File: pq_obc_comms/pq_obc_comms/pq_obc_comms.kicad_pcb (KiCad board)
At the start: 4 copper layers, 40 x 40 mm, 66 parts, among them J1 Conn_01x10, J2 Conn_01x10, J3 Conn_01x10, J4 Conn_01x10, J6 U.FL-R-SMT-1_10_, U1 STM32L476RGTx, U2 SX1262IMLTRT, U3 BD2232G-GTR, U4 BD2232G-GTR, U5 RFswitch, U7 BD2232G-GTR, X1 12MHz, X2 FA-128_32.0000MF20X-K5, X3 32.768KHz

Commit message: obc rework
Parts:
- C1, C10, C11, C12, C2, C4, C5, C6, C7, C8, C9: footprint easyeda:CAPC1005X55N -> Capacitor_SMD:C_0402_1005Metric
- C14, C15, C16, C17, C18: footprint easyeda:CAPC1608X90N -> Capacitor_SMD:C_0603_1608Metric
- C27, C28, C40, C41, C42, C43, C44, C45: footprint easyeda:CAPC1608X90N -> Capacitor_SMD:C_0603_1608Metric; moved to B.Cu
- D1: value VCC -> RBS1LAM40ATR; footprint easyeda:SOD-128_L3.7-W2.5-LS4.7-FD -> Diode_SMD:D_SOD-128; moved to B.Cu
- D2: value VCC_TEST -> RBS1LAM40ATR; footprint easyeda:SOD-128_L3.7-W2.5-LS4.7-FD -> Diode_SMD:D_SOD-128; moved to B.Cu
- J6: value U.FL-R-SMT-1_10_ -> U.FL-R-SMT-1_10; footprint easyeda:U.FL-R-SMT-1(10) -> Connector_Coaxial:U.FL_Hirose_U.FL-R-SMT-1_Vertical
- L1, L3, L4, L5, L6: footprint easyeda:LQW15CNR20J00B -> Inductor_SMD:L_0402_1005Metric
- L2: footprint Resistor_SMD:R_0402_1005Metric -> Inductor_SMD:L_0402_1005Metric
- L7: footprint easyeda:INDC2012X145N -> Inductor_SMD:L_0805_2012Metric
- R3, R4, R6: footprint easyeda:RESC1608X55N -> Resistor_SMD:R_0603_1608Metric
- R7, R8: footprint easyeda:RESC1608X55N -> Resistor_SMD:R_0603_1608Metric; moved to B.Cu
- TP1: renamed from PROBE1; value MS-156C -> CoaxialSwitch_Testpoint; footprint GGS_Connectors:CoaxialSwitch_Hirose_MS-156C3_Horizontal -> Connector_Coaxial:CoaxialSwitch_Hirose_MS-156C3_Horizontal
- U2: footprint easyeda:QFN-24_L4.0-W4.0-P0.50-BL-EP2.6 -> Package_DFN_QFN:QFN-24-1EP_4x4mm_P0.5mm_EP2.6x2.6mm
- U3, U4, U7: footprint easyeda:SSOP-5_L3.0-W1.6-P0.95-LS2.8-TL -> Package_TO_SOT_SMD:SOT-23-5; moved to B.Cu
- U5: value RFswitch -> BGS12PL6E6327XTSA1; footprint easyeda:TSNP-6_L1.1-W0.7-P0.40-BR -> GGS_RF:PG-TSLP-6-4
- X1: value 12MHz -> ECS-120-18-33-JEM-TR3
- X3: value 32.768KHz -> ABS09-32.768KHZ-7-T; footprint easyeda:CRYSTAL-SMD_L4.1-W1.5 -> GGS_Miscellaneous:ABS09; moved to B.Cu
- moved J4 22.9 mm to (110.6, 79.8), turned to -90 degrees
- moved J2 22.9 mm to (82.6, 74.7), turned to 180 degrees
- moved L3 1.03 mm to (108.3, 64.1)
- moved L5 1.03 mm to (104.4, 72.8)
- moved L1 0.99 mm to (108.7, 62.6)
- moved L6 0.95 mm to (106.0, 59.2)
- moved L4 0.94 mm to (108.3, 68.8)
- moved X1 0.16 mm to (85.9, 54.3), turned to -90 degrees
- turned C27 to 0 degrees
- turned C40 to 180 degrees
- turned C41 to 0 degrees
- turned C43 to 0 degrees
- turned C45 to 180 degrees
- turned D1 to 180 degrees
- turned J6 to 180 degrees
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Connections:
- net OSC_OUT renamed /OSC_OUT
- C16 pad 1: VCC_UMBILICAL -> VCC
- C18 pad 1: VCC_UMBILICAL -> VCC
- C31 pad 1: VCC_UMBILICAL -> VCC
- C32 pad 1: VCC_UMBILICAL -> VCC
- C33 pad 1: VCC_UMBILICAL -> VCC
- C34 pad 1: VCC_UMBILICAL -> VCC
- C35 pad 1: VCC_UMBILICAL -> VCC
- C36 pad 1: VCC_UMBILICAL -> VCC
- C37 pad 1: VCC_UMBILICAL -> VCC
- C40 pad 1: unconnected-(C40-Pad1) -> /OSC_IN
- C43 pad 1: VCC_UMBILICAL -> VCC
- C44 pad 1: VCC_UMBILICAL -> VCC
- C45 pad 2: VCC_UMBILICAL -> VCC
- D1 pad 2: VCC_UMBILICAL -> VCC
- D2 pad 1: VCC_TEST2 -> VCC_UMBILICAL
- D2 pad 2: VCC_TEST1 -> VCC
- J1 pad 10: 3V3 -> 3V3_PERM
- J2 pad 1: STM32_PA2 -> SOLAR_X
- J2 pad 10: SOLAR_X -> STM32_PA2
- J2 pad 2: ADC_PL -> unconnected-(J2-Pad2)
- J2 pad 3: DAC_PL -> CLPROG
- J2 pad 4: SWCLK -> CHRGOFF
- J2 pad 5: SWDIO -> NRST
- J2 pad 6: NRST -> SWDIO
- J2 pad 7: CHRGOFF -> SWCLK
- J2 pad 8: CLPROG -> DAC_PL
- J2 pad 9: MPPT_X -> ADC_PL
- J3 pad 10: EPS_RST -> unconnected-(J3-Pad10)
- J3 pad 3: STM32_PD2 -> BATT_NTC
- J4 pad 1: CHRG -> SOLAR_Z
- J4 pad 10: SOLAR_Z -> CHRG
- J4 pad 2: FAULT -> STM32_PD2
- J4 pad 3: VCC_UMBILICAL -> ADCS_POWER
- J4 pad 4: SEL_PH0 -> RST_DRIVERS
- J4 pad 5: P/L_POWER -> ADC_PH
- J4 pad 6: ADC_PH -> P/L_POWER
- J4 pad 7: RST_DRIVERS -> SEL_PH0
- J4 pad 8: MPPT_Y -> VCC_UMBILICAL
- J4 pad 9: MPPT_Z -> FAULT
- J6 pad 1: GND -> Net-(C10-Pad1)
- R4 pad 1: VCC_UMBILICAL -> VCC
- R7 pad 1: VCC_UMBILICAL -> VCC
- R8 pad 1: VCC_UMBILICAL -> VCC
- U1 pad 1: VCC_UMBILICAL -> VCC
- U1 pad 13: VCC_UMBILICAL -> VCC
- U1 pad 19: VCC_UMBILICAL -> VCC
- U1 pad 32: VCC_UMBILICAL -> VCC
- U1 pad 48: VCC_UMBILICAL -> VCC
- U1 pad 5: OSC_IN -> /OSC_IN
- U1 pad 64: VCC_UMBILICAL -> VCC
- U2 pad 1: VCC_UMBILICAL -> VCC
- U2 pad 10: VCC_UMBILICAL -> VCC
- U2 pad 11: VCC_UMBILICAL -> VCC
- U3 pad 1: VCC_UMBILICAL -> VCC
- U4 pad 1: VCC_UMBILICAL -> VCC
- U4 pad 5: P/L2BURN -> ADCS_POWER
- U7 pad 1: VCC_UMBILICAL -> VCC
- X1 pad 1: OSC_IN -> /OSC_IN
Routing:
- net VCC_UMBILICAL: track 149.6 -> 2.70 mm, vias 5 -> 0
- net VCC: track 0.00 -> 138.6 mm, vias 0 -> 5
- net SOLAR_Z: track 0.00 -> 37.1 mm
- net EPS_RST: track 37.1 -> 0.00 mm
- net ADCS_POWER: track 0.00 -> 25.3 mm
- net STM32_PD2: track 25.3 -> 49.0 mm
- net MPPT_Z: track 23.8 -> 0.00 mm
- net MPPT_Y: track 21.8 -> 0.00 mm
- net CHRGOFF: track 14.6 -> 0.00 mm, vias 1 -> 0
- net CHGOFF: track 0.00 -> 14.6 mm, vias 0 -> 1
- net 3V3: track 0.00 -> 8.38 mm
- net OSC32_IN: track 15.0 -> 7.01 mm, vias 2 -> 1
- net /OSC_IN: track 0.00 -> 7.98 mm, vias 0 -> 1
- net STM32_PA15: track 3.45 -> 0.00 mm
- net GND: track 7.92 -> 6.07 mm, vias 59 -> 58
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
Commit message: OBC board revision 3 finished
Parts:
- added C3: 100nF, Capacitor_SMD:C_0603_1608Metric, F.Cu at (104.1, 48.5)
- C27, C28, C31, C32, C33, C34, C35, C36, C37, R7, R8: moved to F.Cu
- X2: footprint easyeda:FA128320000MF20XK5 -> GGS_Miscellaneous:EPSON_FA128
- moved C27 26.5 mm to (112.4, 47.4)
- moved X2 26.3 mm to (112.4, 49.7), turned to -90 degrees
- moved C35 25.6 mm to (100.1, 51.3), turned to 0 degrees
- moved C36 24.0 mm to (87.4, 51.3)
- moved C28 23.5 mm to (112.4, 52.0), turned to 180 degrees
- moved C34 22.9 mm to (87.4, 49.8)
- moved U4 22.2 mm to (104.4, 72.1), turned to -90 degrees
- moved C44 18.5 mm to (104.2, 69.3), turned to 0 degrees
- moved C37 17.7 mm to (100.0, 63.5), turned to 0 degrees
- moved C38 10.8 mm to (86.4, 48.9), turned to 90 degrees
- moved C39 9.50 mm to (92.7, 48.9)
- moved C41 8.53 mm to (94.3, 55.9), turned to 90 degrees
- moved X3 8.06 mm to (89.5, 49.7), turned to 0 degrees
- moved C43 7.71 mm to (108.7, 69.3)
- moved D1 5.96 mm to (109.2, 46.8)
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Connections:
- net Net-(R3-Pad1) renamed /DIO2
- net Net-(U5-Pad4) renamed /RFswitch_Vcc
- D1 pad 1: 3V3 -> 3V3_PERM
- J3 pad 10: unconnected-(J3-Pad10) -> GND
- J4 pad 2: STM32_PD2 -> STM32_PB0
- U1 pad 10: SEL_PH3 -> SEL_PH0
- U1 pad 11: /PoL_P/L_EN -> unconnected-(U1-Pad11)
- U1 pad 22: MPPT_X -> unconnected-(U1-Pad22)
- U1 pad 23: MPPT_Z -> /PoL_ADCS_POWER_EN
- U1 pad 26: EPS_RST -> STM32_PB0
- U1 pad 27: MPPT_Y -> unconnected-(U1-Pad27)
- U1 pad 37: unconnected-(U1-Pad37) -> /PoL_P/L_EN
- U1 pad 41: /BUSY -> /SX1262_BUSY
- U1 pad 54: STM32_PD2 -> unconnected-(U1-Pad54)
- U1 pad 8: CHGOFF -> CHRGOFF
- U4 pad 3: P/L2BURN_OBC -> /PoL_ADCS_POWER_EN
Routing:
- net VCC: track 138.6 -> 63.3 mm, vias 5 -> 18
- net STM32_PD2: track 49.0 -> 0.00 mm, vias 1 -> 0
- net /XTB: track 48.8 -> 9.60 mm, vias 2 -> 0
- net SOLAR_Z: track 37.1 -> 0.00 mm
- net unconnected-(U1-Pad17): track 33.5 -> 0.00 mm, vias 2 -> 0
- net STM32_PB0: track 0.00 -> 32.9 mm, vias 0 -> 2
- net STM32_PA15: track 0.00 -> 25.9 mm, vias 0 -> 2
- net /PoL_ADCS_POWER_EN: track 0.00 -> 25.9 mm, vias 0 -> 1
- net ADCS_POWER: track 25.3 -> 4.79 mm
- net /PoL_P/L_EN: track 34.2 -> 17.0 mm, vias 2 -> 3
- net /XTA: track 23.5 -> 6.70 mm, vias 2 -> 0
- net P/L2BURN_OBC: track 16.5 -> 0.00 mm, vias 1 -> 0
- net CHGOFF: track 14.6 -> 0.00 mm, vias 1 -> 0
- net /DIO2: track 19.4 -> 33.4 mm, vias 2 -> 3
- net MPPT_X: track 14.0 -> 0.00 mm
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- added copper zone on B.Cu, net VCC
- added copper zone on In2.Cu, net VCC
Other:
- board text removed: "12MHz"
- board text removed: "32.7KHz"
- board text removed: "32MHz"
- board text removed: "BD2232G"
- board text removed: "BurnCOMMS"
- board text removed: "D-VCC"
- board text removed: "D-VCCTest"
- board text removed: "OBC-COMMS"
- board text removed: "PL2BURN"
- board text removed: "PL2VCC"
- board text removed: "STM32L162RE"
- board text removed: "SX1262"

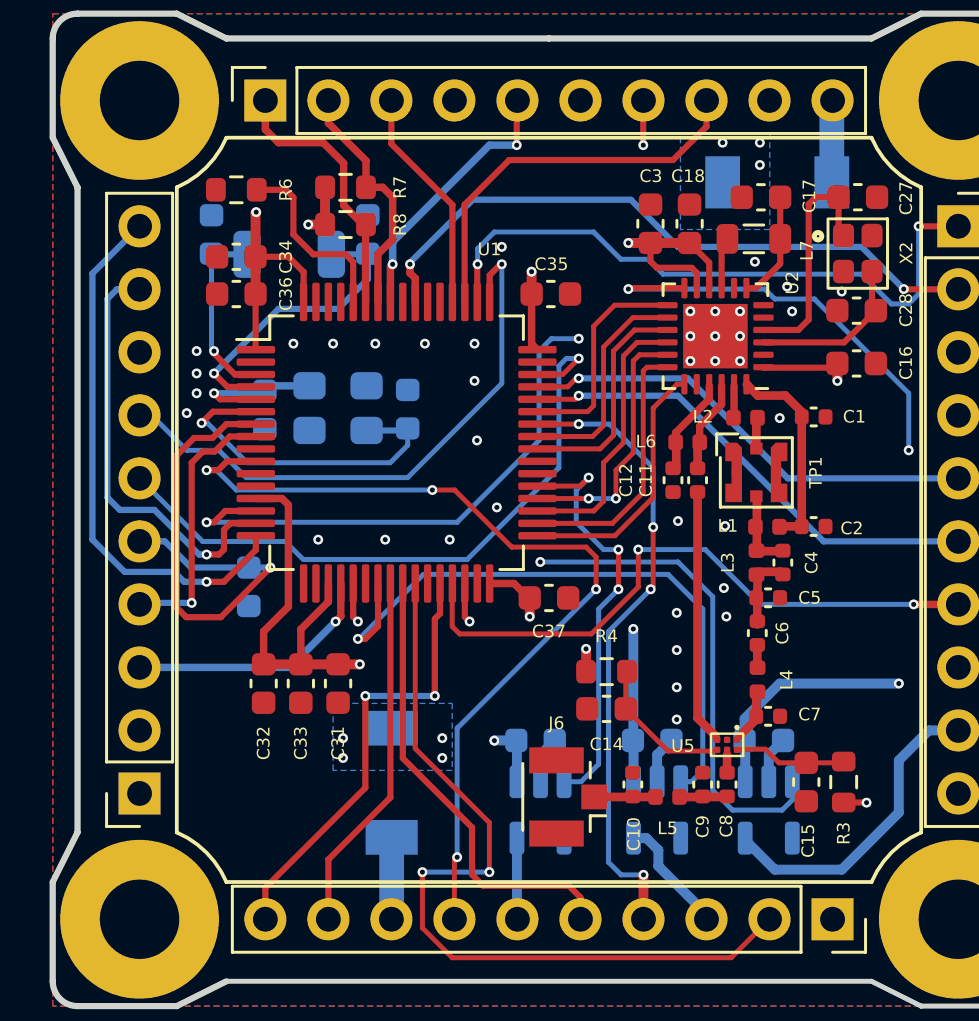
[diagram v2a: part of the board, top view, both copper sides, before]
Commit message: added PA3 pin to pinout
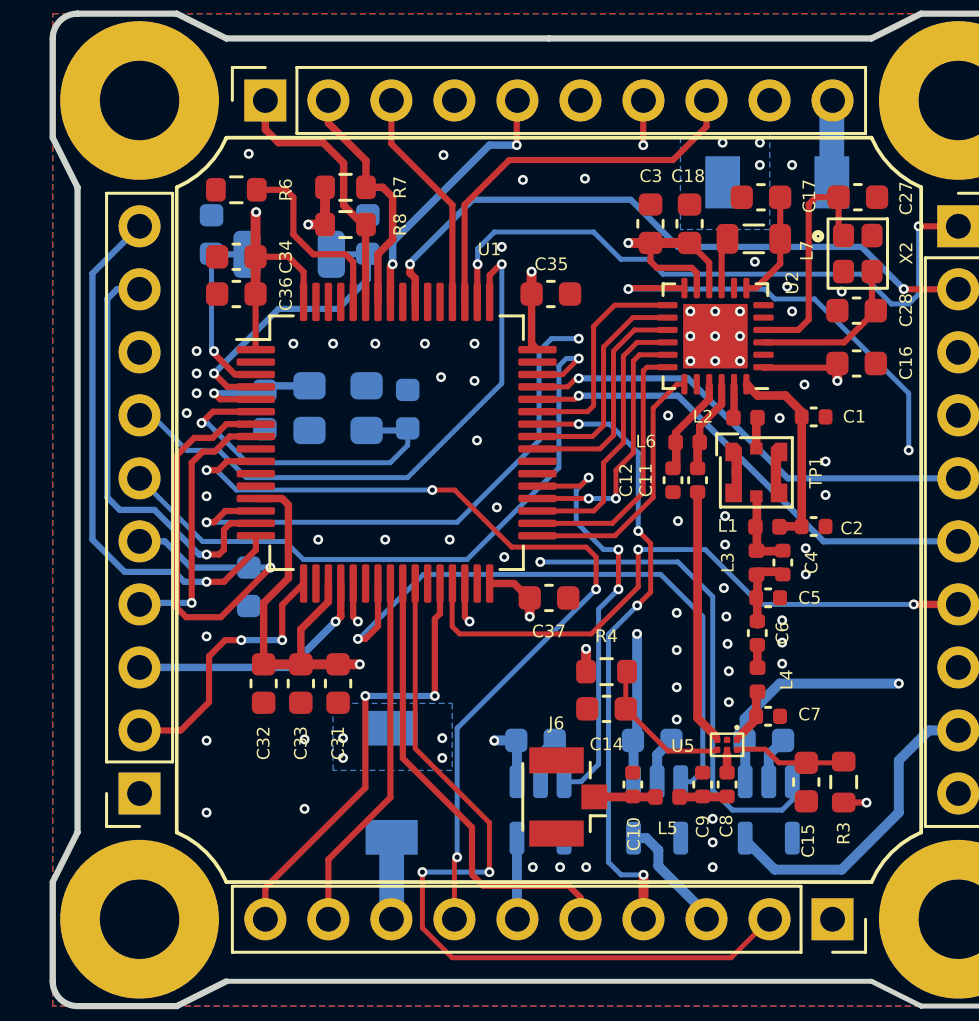
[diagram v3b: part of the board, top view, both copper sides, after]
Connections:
- J2 pad 2: unconnected-(J2-Pad2) -> STM32_PA3
- U1 pad 17: unconnected-(U1-Pad17) -> STM32_PA3
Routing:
- net STM32_PA3: track 0.00 -> 11.0 mm, vias 0 -> 2
- net GND: vias 38 -> 70

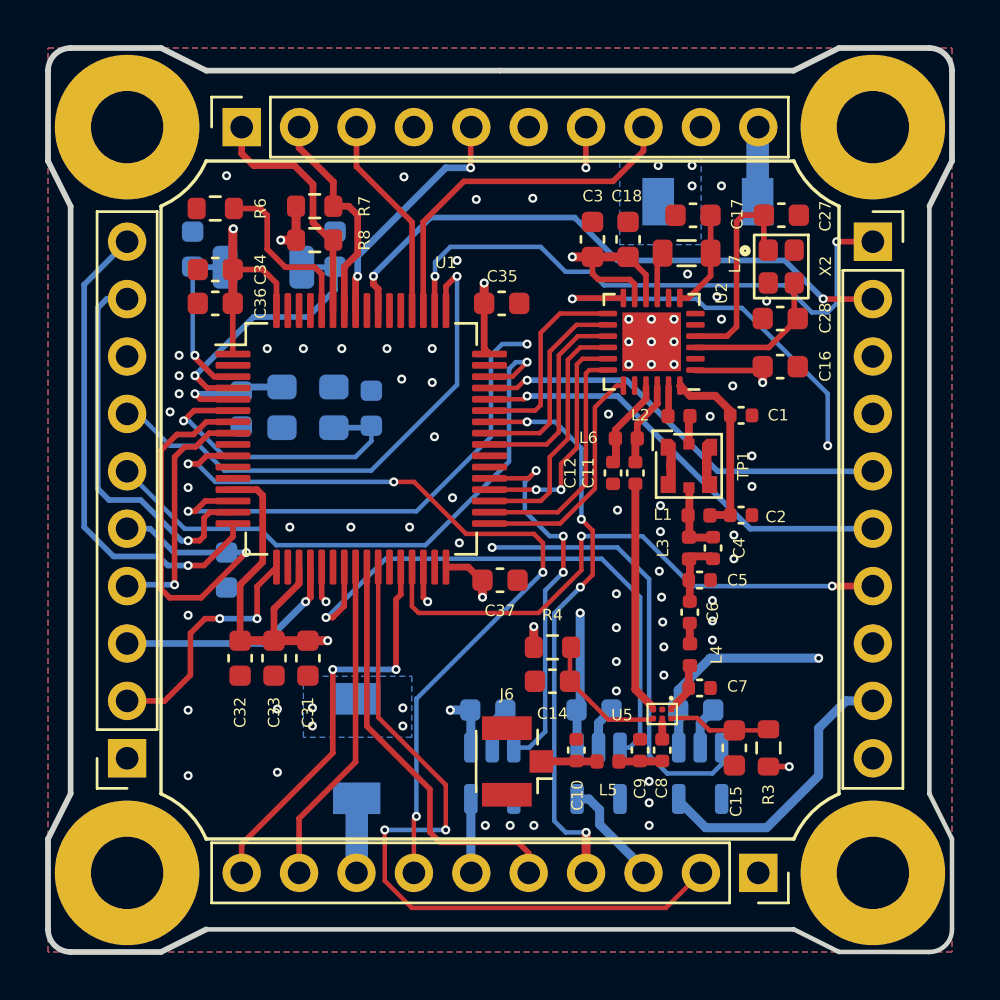
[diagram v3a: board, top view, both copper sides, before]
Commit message: OBC finished, BoM included and RF traces revised
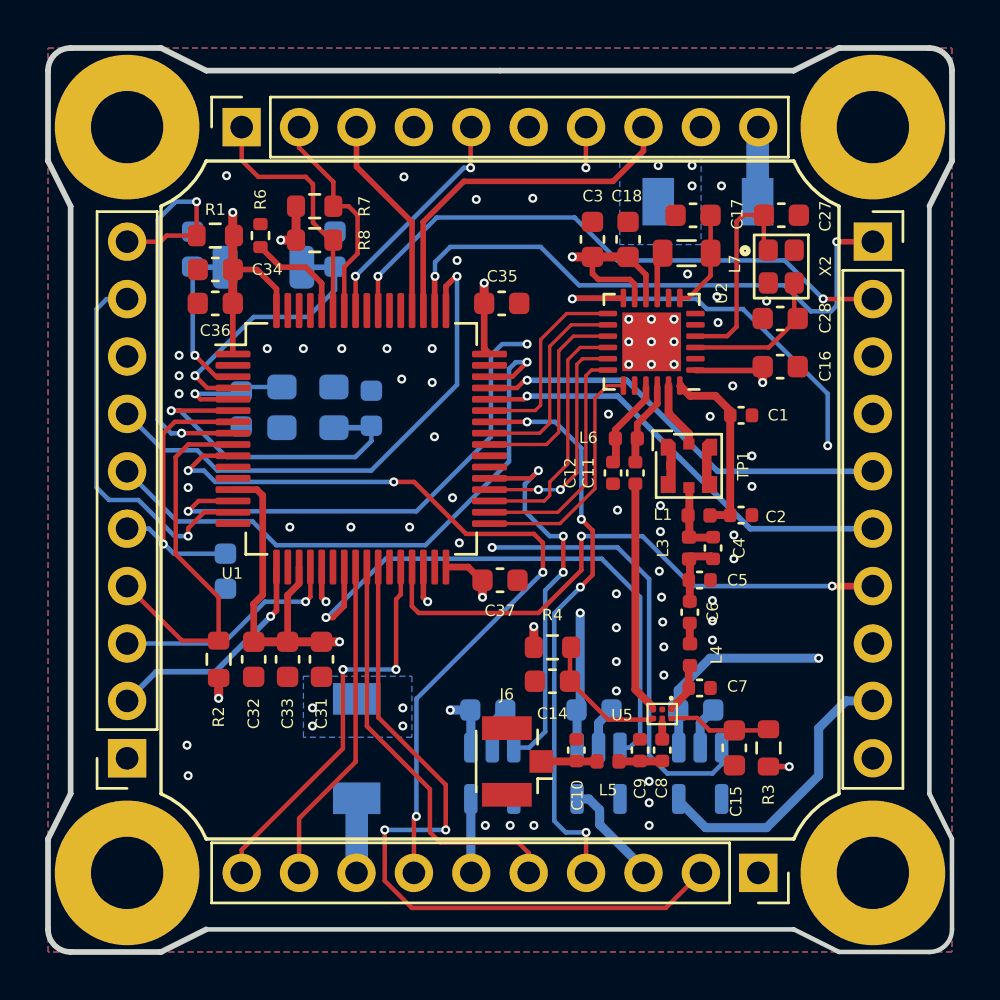
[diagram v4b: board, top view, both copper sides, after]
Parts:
- removed L2: 0R, Inductor_SMD:L_0402_1005Metric
- added R1: 4.7k, Resistor_SMD:R_0603_1608Metric, F.Cu at (87.4, 48.3)
- added R2: 4.7k, Resistor_SMD:R_0603_1608Metric, F.Cu at (87.5, 67.0)
- R6: footprint Resistor_SMD:R_0603_1608Metric -> Resistor_SMD:R_0402_1005Metric
- moved R6 2.33 mm to (89.4, 48.3), turned to 90 degrees
- moved C31 0.60 mm to (92.1, 67.0)
- moved C32 0.60 mm to (89.1, 67.0)
- moved C33 0.60 mm to (90.6, 67.0)
- moved C42 0.07 mm to (87.8, 63.1)
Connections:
- net SCL renamed SCL1
- net SDA renamed SDA1
- J2 pad 10: STM32_PA2 -> SCL3
- J2 pad 2: STM32_PA3 -> CHRGOFF
- J2 pad 4: CHRGOFF -> SDA3
- TP1 pad C: Net-(L2-Pad2) -> Net-(TP1-PadC)
- U1 pad 16: STM32_PA2 -> unconnected-(U1-Pad16)
- U1 pad 17: STM32_PA3 -> CHRGOFF
- U1 pad 8: CHRGOFF -> SCL3
- U1 pad 9: unconnected-(U1-Pad9) -> SDA3
- U2 pad 23: Net-(L2-Pad1) -> Net-(TP1-PadC)
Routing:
- net STM32_PA2: track 21.8 -> 0.00 mm, vias 1 -> 0
- net SCL3: track 0.00 -> 19.2 mm, vias 0 -> 2
- net SDA3: track 0.00 -> 16.7 mm
- net STM32_PA3: track 11.0 -> 0.00 mm, vias 2 -> 0
- net NRST: track 20.3 -> 13.0 mm
- net /Boot0: track 7.58 -> 4.58 mm
- net Net-(TP1-PadC): track 0.00 -> 2.97 mm
- net Net-(L2-Pad1): track 1.26 -> 0.00 mm
- net Net-(L2-Pad2): track 1.26 -> 0.00 mm
- net /OSC_OUT: track 13.9 -> 15.0 mm
- net VCC: track 63.2 -> 64.1 mm, vias 18 -> 19
- net CHRGOFF: track 10.8 -> 10.2 mm
- net GND: vias 70 -> 66

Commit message: lots of changes
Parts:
- added C13: 1uF, Capacitor_SMD:C_0603_1608Metric, B.Cu at (111.0, 68.2)
- added REF**: bike_small, GGS_Symbols:bike_small, B.Cu at (88.8, 74.3)
- added U6: BD2232G-GTR, Package_TO_SOT_SMD:SOT-23-5, B.Cu at (112.3, 65.0)
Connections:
- J3 pad 7: HEATER_EN -> GND
- U1 pad 29: HEATER_EN -> /HEATER_EN
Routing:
- net HEATER_EN: track 25.5 -> 0.00 mm, vias 2 -> 0
- net /HEATER_EN: track 0.00 -> 20.2 mm, vias 0 -> 1
- net HEATER_PWR: track 0.00 -> 3.23 mm
- net GND: track 5.70 -> 7.40 mm
- net VCC: track 64.1 -> 65.5 mm
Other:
- board text added: "OBC&COMMS"

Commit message: document formating
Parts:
- moved J4 61.0 mm to (161.4, 111.5)
- moved X3 61.0 mm to (139.5, 84.7)
- moved TP1 61.0 mm to (158.4, 93.5)
- moved X2 61.0 mm to (162.4, 84.7)
- moved D2 61.0 mm to (143.7, 106.0)
- moved J2 61.0 mm to (133.5, 106.4)
- moved C15 61.0 mm to (160.4, 106.0)
- moved C31 61.0 mm to (142.1, 102.0)
- moved C32 61.0 mm to (139.1, 102.0)
- moved C33 61.0 mm to (140.6, 102.0)
- moved C42 61.0 mm to (137.9, 98.2)
- moved C8 61.0 mm to (157.2, 106.1)
- moved U1 61.0 mm to (143.9, 92.3)
- moved U4 61.0 mm to (154.4, 107.1)
- moved U7 61.0 mm to (158.9, 107.1)
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
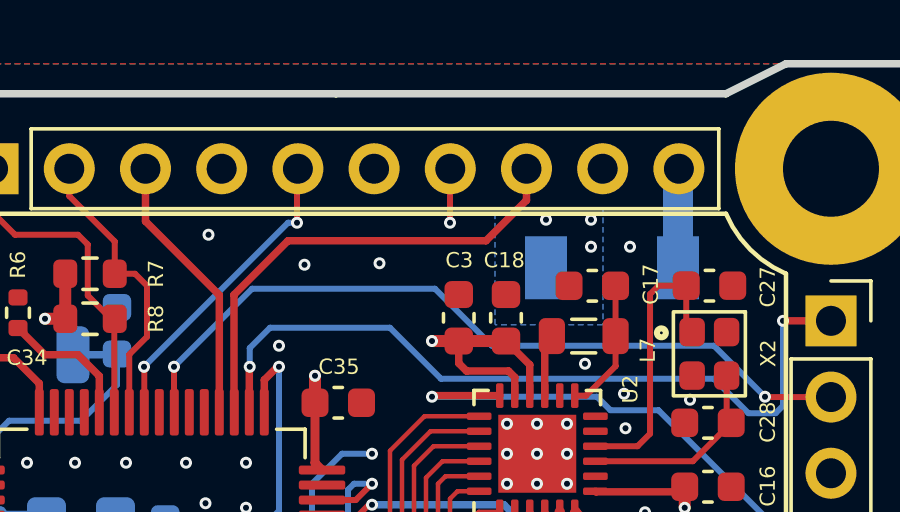
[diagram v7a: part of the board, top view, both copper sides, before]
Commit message: ADCS: added magnetometer, removed Tsens. OBC: Total_Current net removed, Bat_NTC routed to PA0 OBC ADC input. Ymag: centering of the vertical pin
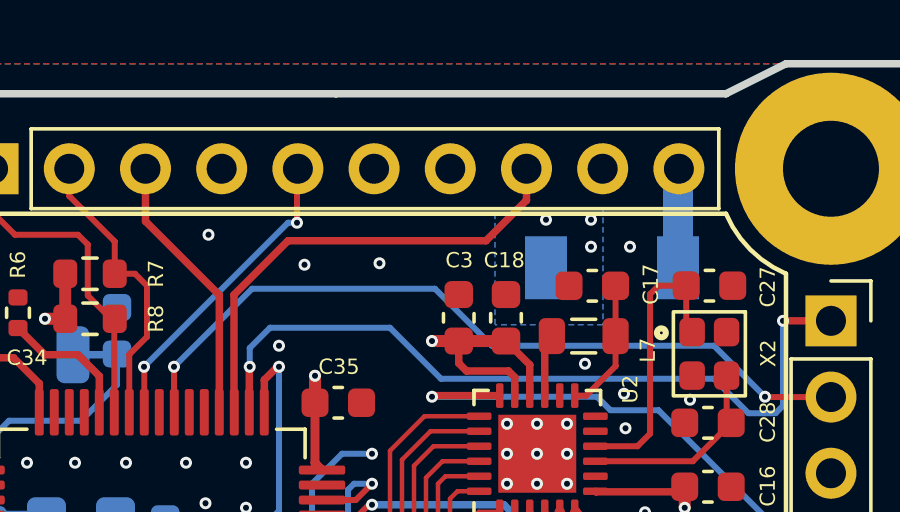
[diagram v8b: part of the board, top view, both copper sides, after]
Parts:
- removed REF**: bike_small, GGS_Symbols:bike_small
- J6: value U.FL-R-SMT-1_10 -> U.FL
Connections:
- J1 pad 7: TOTAL_CURRENT -> NC
- U1 pad 14: TOTAL_CURRENT -> BATT_NTC
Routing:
- net BATT_NTC: track 0.00 -> 41.2 mm, vias 0 -> 2
- net TOTAL_CURRENT: track 33.0 -> 0.00 mm, vias 3 -> 0
